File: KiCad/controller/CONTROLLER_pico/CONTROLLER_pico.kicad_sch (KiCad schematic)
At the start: 5 parts, among them J3 jack2.5_PJ-210B, J4 Conn_01x20_Male, J5 Conn_01x20_Male, J6 Conn_01x03_Male, J7 Conn_01x03_Male

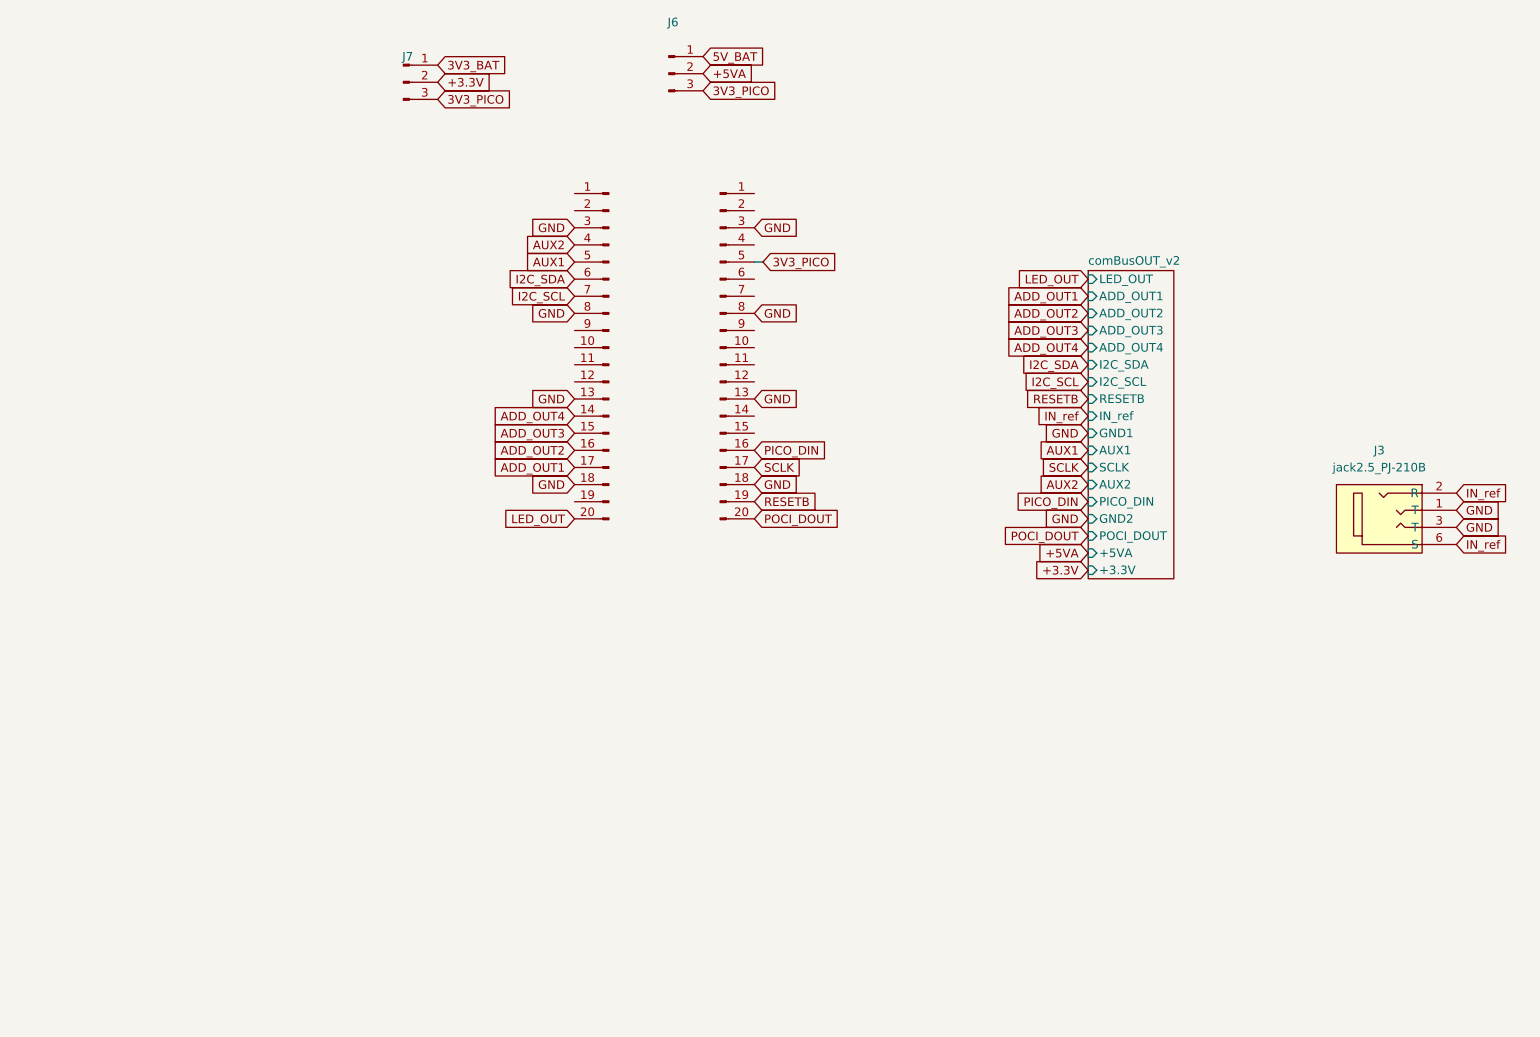
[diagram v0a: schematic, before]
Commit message: fixed pico controller shield to match v3 modules
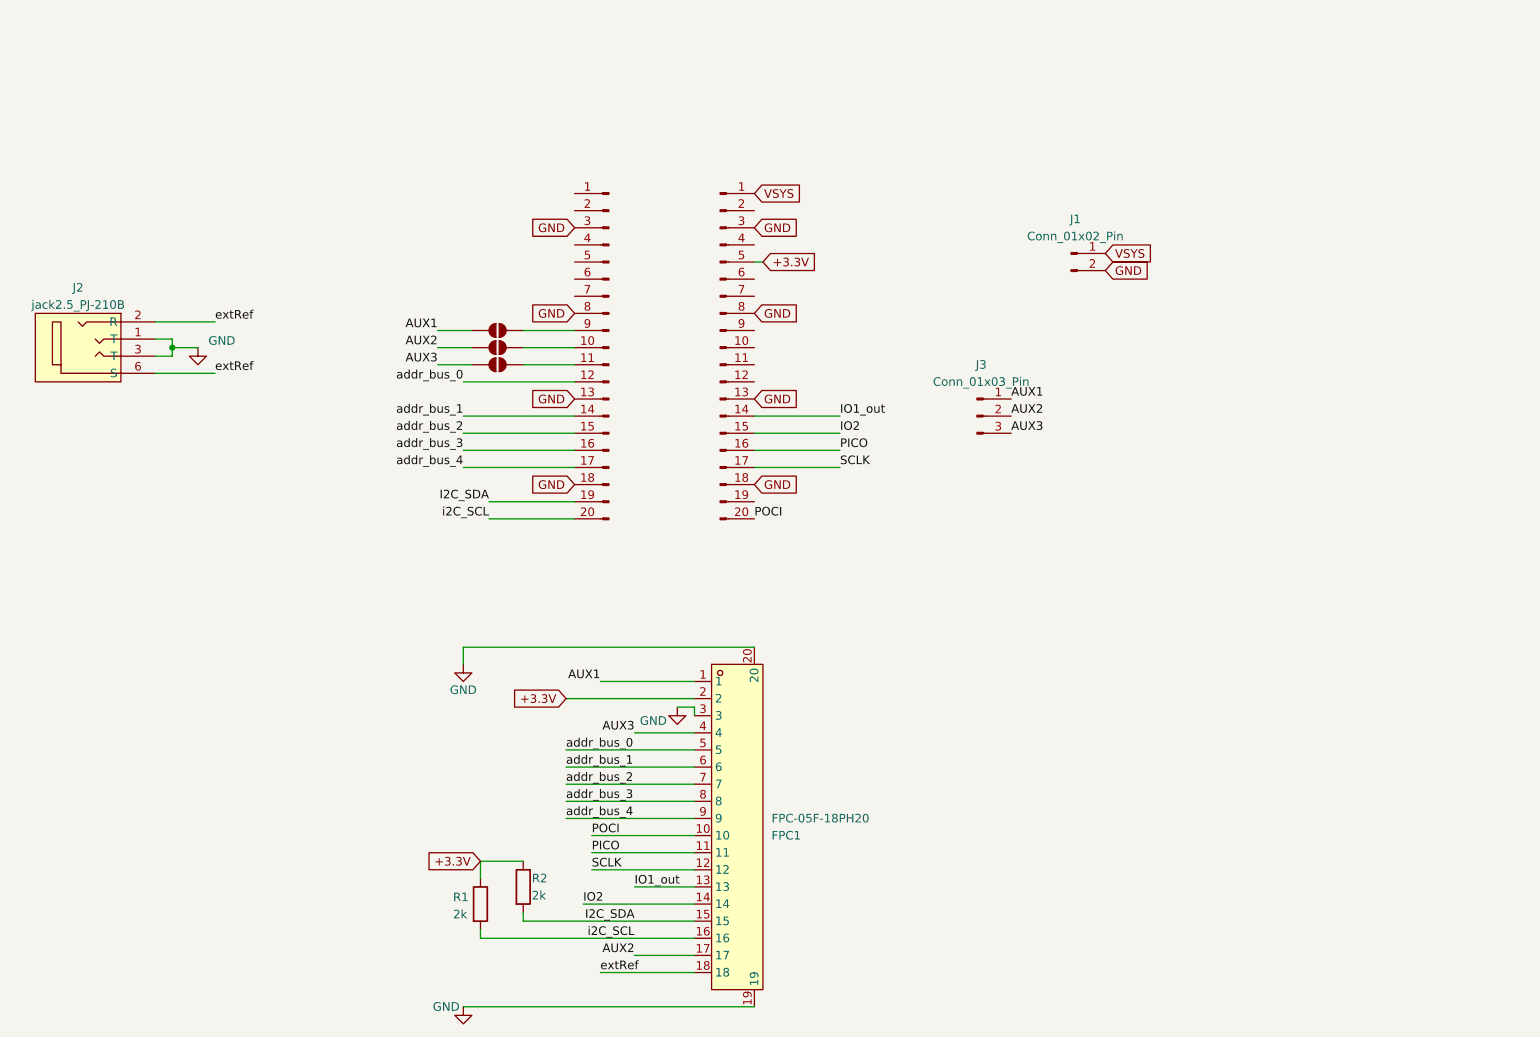
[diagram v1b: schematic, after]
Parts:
- removed J3: jack2.5_PJ-210B, 00_custom-footprints:Jack_Socket_PJ-210B, symbol 00_custom:jack2.5_PJ-210B
- removed J6, J7: Conn_01x03_Male, Connector_PinHeader_2.54mm:PinHeader_1x03_P2.54mm_Vertical, symbol Connector:Conn_01x03_Male
- added FPC1: FPC-05F-18PH20, 00_lcsc:FPC-SMD_18P-P0.50_X05C2018TZ, symbol 00_lcsc:FPC-05F-18PH20
- added J1: Conn_01x02_Pin, Connector_PinHeader_1.27mm:PinHeader_1x02_P1.27mm_Vertical, symbol Connector:Conn_01x02_Pin
- added J2: jack2.5_PJ-210B, 00_custom-footprints:Jack_Socket_PJ-210B, symbol 00_custom:jack2.5_PJ-210B
- added J3: Conn_01x03_Pin, Connector_PinSocket_1.27mm:PinSocket_1x03_P1.27mm_Vertical, symbol Connector:Conn_01x03_Pin
- added JP2, JP3, JP4: SolderJumper_2_Open, Jumper:SolderJumper-2_P1.3mm_Open_TrianglePad1.0x1.5mm, symbol Jumper:SolderJumper_2_Open
- added R1, R2: 2k, Resistor_SMD:R_0402_1005Metric_Pad0.72x0.64mm_HandSolder, symbol Device:R
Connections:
- net 3V3_PICO is gone; now on net +3.3V: J5.5 (Pin_5)
- net +3.3V: now also FPC1.2, R1.1, R2.1
- net AUX1: now also FPC1.1, J3.1 (Pin_1), JP2.1 (A); no longer J4.5 (Pin_5)
- net AUX2: now also FPC1.17, J3.2 (Pin_2), JP3.1 (A); no longer J4.4 (Pin_4)
- net GND: now also FPC1.19, FPC1.20, FPC1.3, J1.2 (Pin_2), J2.1 (T), J2.3 (T)
- net I2C_SDA: now also J4.19 (Pin_19), FPC1.15, R2.2; no longer J4.6 (Pin_6)
- net SCLK: now also FPC1.12
- net at J4.10 (Pin_10): now also JP3.2 (B)
- net at J4.11 (Pin_11): now also JP4.2 (B)
- net addr_bus_0: now reaches J4.12 (Pin_12)
- net addr_bus_0: now also FPC1.5
- net at J4.9 (Pin_9): now also JP2.2 (B)
- net VSYS: now reaches J5.1 (Pin_1)
- net VSYS: now also J1.1 (Pin_1)
- net IO1_out: now reaches J5.14 (Pin_14)
- net IO1_out: now also FPC1.13
- net IO2: now reaches J5.15 (Pin_15)
- net IO2: now also FPC1.14
- net ADD_OUT1 renamed addr_bus_4
- net addr_bus_4: now also FPC1.9
- net ADD_OUT2 renamed addr_bus_3
- net addr_bus_3: now also FPC1.8
- net ADD_OUT3 renamed addr_bus_2
- net addr_bus_2: now also FPC1.7
- net ADD_OUT4 renamed addr_bus_1
- net addr_bus_1: now also FPC1.6
- net I2C_SCL: no longer names the net of J4.7 (Pin_7)
- net LED_OUT renamed i2C_SCL
- net i2C_SCL: now also FPC1.16, R1.2
- net PICO_DIN renamed PICO
- net PICO: now also FPC1.11
- net POCI_DOUT renamed POCI
- net POCI: now also FPC1.10
- net RESETB: no longer names the net of J5.19 (Pin_19)
- new net AUX3: FPC1.4, J3.3 (Pin_3), JP4.1 (A)
- new net extRef: FPC1.18, J2.2 (R), J2.6 (S)
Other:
- removed sheet comBusOUT_v2
